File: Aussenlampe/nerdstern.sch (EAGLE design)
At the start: 14 parts, among them K1 G6RS

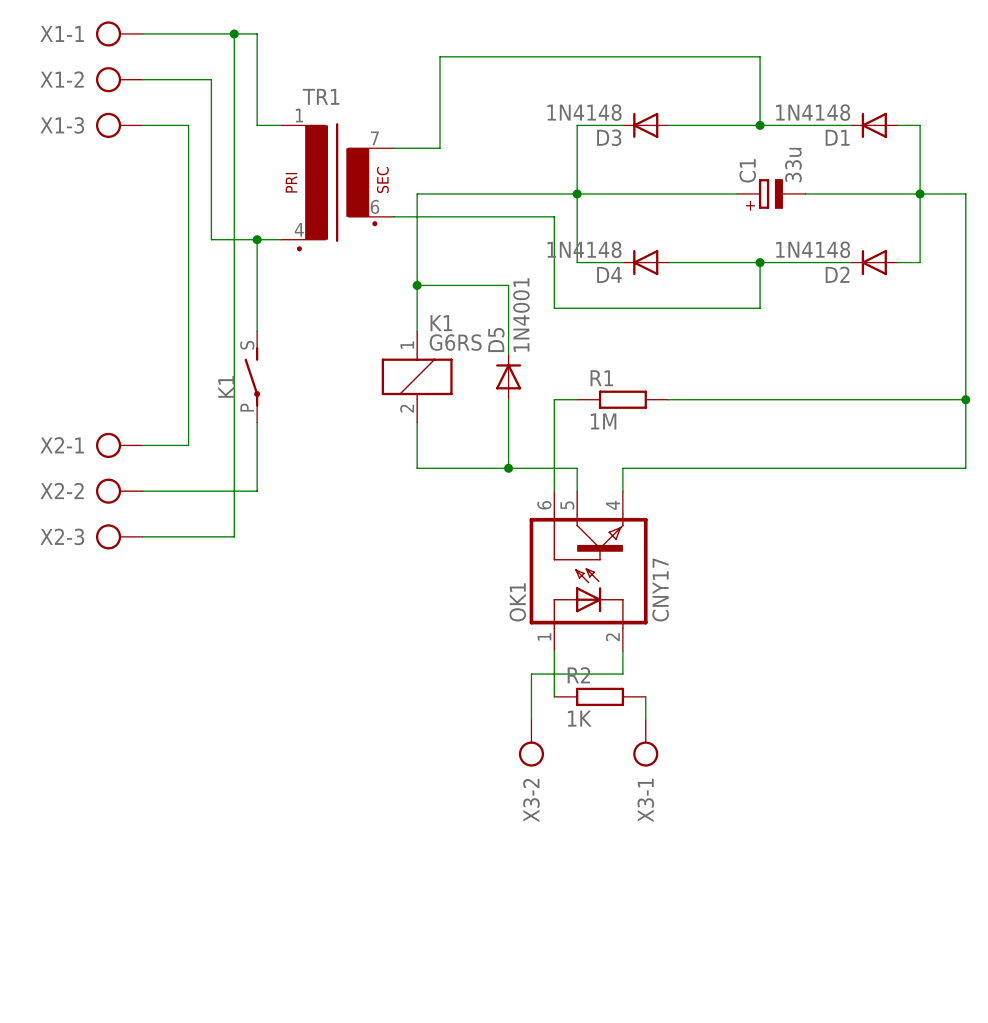
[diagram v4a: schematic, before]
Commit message: modified .gitignore
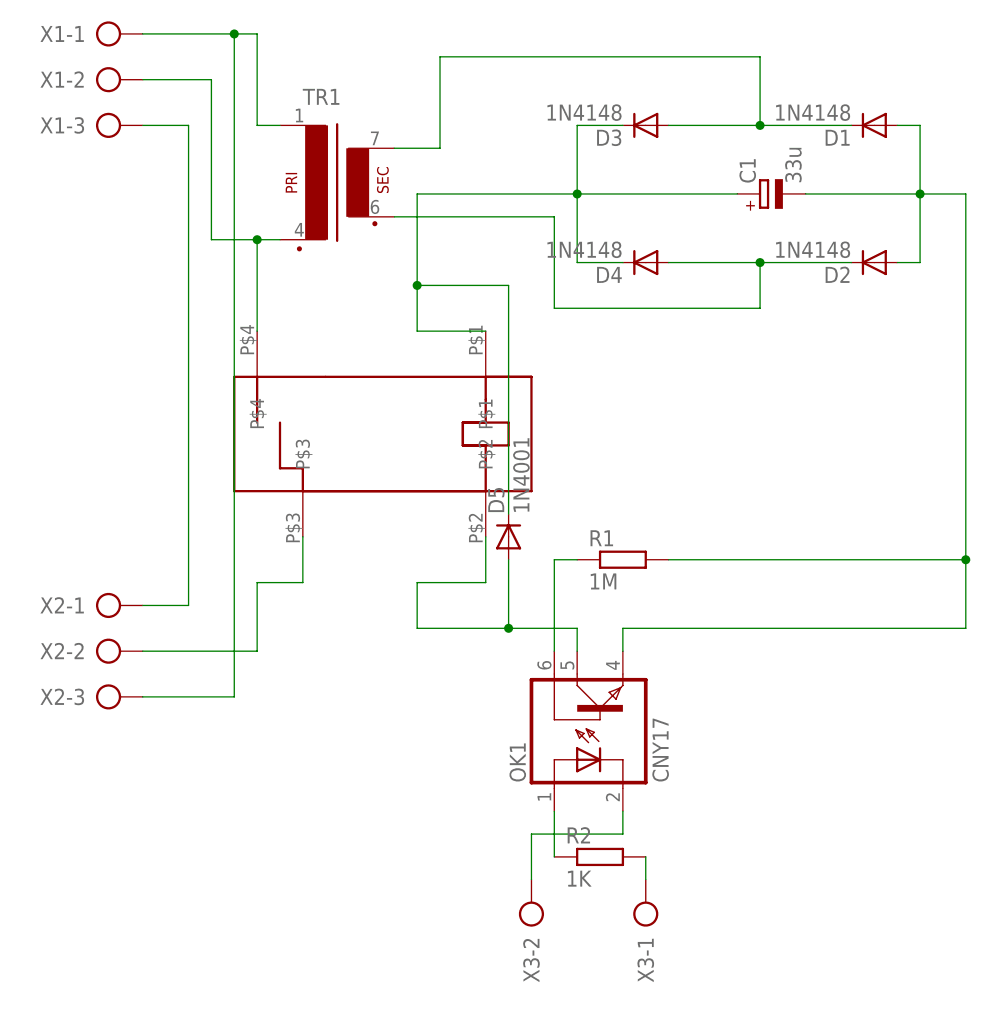
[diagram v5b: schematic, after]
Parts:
- removed K1: G6RS, relay:G6RS
- added U$1: JS_05_MN_KT, n39:JS_05_MN_KT
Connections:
- removed net N$12: D5.A, K11.2, OK1.COL
- new net N$6: D5.A, OK1.COL, U$1.P$2
- net N$1: now also U$1.P$4; no longer K12.S
- net N$2: now also U$1.P$3; no longer K12.P
- net N$5: now also U$1.P$1; no longer K11.1
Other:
- moved on the sheet: D5, OK1, R1, R2, X2-1, X2-2, X2-3, X3-1, X3-2
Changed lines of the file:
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@@
 <part name="D4" library="diode" deviceset="1N4148" device="DO35-7" value="1N4148"/>
 <part name="C1" library="rcl" deviceset="CPOL-EU" device="E2-5" value="33u"/>
-<part name="K1" library="relay" deviceset="G6RS" device=""/>
 <part name="X1" library="con-ptr500" deviceset="AK500/3" device=""/>
 <part name="X2" library="con-ptr500" deviceset="AK500/3" device=""/>
@@
 <part name="R2" library="rcl" deviceset="R-EU_" device="0204/5" value="1K"/>
 <part name="D5" library="diode" deviceset="1N4148" device="DO35-7" value="1N4001"/>
+<part name="U$1" library="n39" deviceset="JS_05_MN_KT" device=""/>
 </parts>
 <sheets>
@@
 <instance part="D4" gate="G$1" x="66.04" y="58.42" rot="R180"/>
 <instance part="C1" gate="G$1" x="78.74" y="66.04" rot="R90"/>
-<instance part="K1" gate="1" x="40.64" y="45.72"/>
-<instance part="K1" gate="2" x="22.86" y="45.72"/>
 <instance part="X1" gate="-1" x="5.08" y="83.82"/>
 <instance part="X1" gate="-2" x="5.08" y="78.74"/>
 <instance part="X1" gate="-3" x="5.08" y="73.66"/>
-<instance part="X2" gate="-1" x="5.08" y="38.1"/>
-<instance part="X2" gate="-2" x="5.08" y="33.02"/>
-<instance part="X2" gate="-3" x="5.08" y="27.94"/>
-<instance part="X3" gate="-1" x="66.04" y="2.54" rot="R90"/>
-<instance part="X3" gate="-2" x="53.34" y="2.54" rot="R90"/>
-<instance part="OK1" gate="G$1" x="58.42" y="25.4" rot="R90"/>
-<instance part="R1" gate="G$1" x="63.5" y="43.18"/>
-<instance part="R2" gate="G$1" x="60.96" y="10.16"/>
-<instance part="D5" gate="G$1" x="50.8" y="45.72" rot="R90"/>
+<instance part="X2" gate="-1" x="5.08" y="20.32"/>
+<instance part="X2" gate="-2" x="5.08" y="15.24"/>
+<instance part="X2" gate="-3" x="5.08" y="10.16"/>
+<instance part="X3" gate="-1" x="66.04" y="-15.24" rot="R90"/>
+<instance part="X3" gate="-2" x="53.34" y="-15.24" rot="R90"/>
+<instance part="OK1" gate="G$1" x="58.42" y="7.62" rot="R90"/>
+<instance part="R1" gate="G$1" x="63.5" y="25.4"/>
+<instance part="R2" gate="G$1" x="60.96" y="-7.62"/>
+<instance part="D5" gate="G$1" x="50.8" y="27.94" rot="R90"/>
+<instance part="U$1" gate="G$1" x="53.34" y="45.72" rot="R180"/>
 </instances>
 <busses>
@@
 <pinref part="TR1" gate="1" pin="P2"/>
 <wire x1="17.78" y1="60.96" x2="22.86" y2="60.96" width="0.1524" layer="91"/>
-<pinref part="K1" gate="2" pin="S"/>
 <wire x1="22.86" y1="50.8" x2="22.86" y2="60.96" width="0.1524" layer="91"/>
 <wire x1="22.86" y1="60.96" x2="25.4" y2="60.96" width="0.1524" layer="91"/>
 <junction x="22.86" y="60.96"/>
+<pinref part="U$1" gate="G$1" pin="P$4"/>
 </segment>
 </net>
 <net name="N$2" class="0">
 <segment>
-<pinref part="K1" gate="2" pin="P"/>
-<wire x1="22.86" y1="40.64" x2="22.86" y2="33.02" width="0.1524" layer="91"/>
-<wire x1="22.86" y1="33.02" x2="10.16" y2="33.02" width="0.1524" layer="91"/>
+<wire x1="22.86" y1="22.86" x2="22.86" y2="15.24" width="0.1524" layer="91"/>
+<wire x1="22.86" y1="15.24" x2="10.16" y2="15.24" width="0.1524" layer="91"/>
 <pinref part="X2" gate="-2" pin="KL"/>
+<pinref part="U$1" gate="G$1" pin="P$3"/>
+<wire x1="22.86" y1="22.86" x2="27.94" y2="22.86" width="0.1524" layer="91"/>
+<wire x1="27.94" y1="22.86" x2="27.94" y2="27.94" width="0.1524" layer="91"/>
 </segment>
 </net>
@@
 <wire x1="22.86" y1="83.82" x2="20.32" y2="83.82" width="0.1524" layer="91"/>
 <wire x1="20.32" y1="83.82" x2="10.16" y2="83.82" width="0.1524" layer="91"/>
-<wire x1="20.32" y1="27.94" x2="20.32" y2="83.82" width="0.1524" layer="91"/>
+<wire x1="20.32" y1="10.16" x2="20.32" y2="83.82" width="0.1524" layer="91"/>
 <junction x="20.32" y="83.82"/>
 <pinref part="X2" gate="-3" pin="KL"/>
-<wire x1="20.32" y1="27.94" x2="10.16" y2="27.94" width="0.1524" layer="91"/>
+<wire x1="20.32" y1="10.16" x2="10.16" y2="10.16" width="0.1524" layer="91"/>
 </segment>
 </net>
@@
 <net name="N$5" class="0">
 <segment>
-<pinref part="K1" gate="1" pin="1"/>
 <wire x1="40.64" y1="50.8" x2="40.64" y2="55.88" width="0.1524" layer="91"/>
 <pinref part="C1" gate="G$1" pin="+"/>
@@
 <wire x1="40.64" y1="66.04" x2="58.42" y2="66.04" width="0.1524" layer="91"/>
 <junction x="58.42" y="66.04"/>
-<wire x1="50.8" y1="48.26" x2="50.8" y2="55.88" width="0.1524" layer="91"/>
+<wire x1="50.8" y1="30.48" x2="50.8" y2="55.88" width="0.1524" layer="91"/>
 <wire x1="50.8" y1="55.88" x2="40.64" y2="55.88" width="0.1524" layer="91"/>
 <junction x="40.64" y="55.88"/>
 <pinref part="D5" gate="G$1" pin="C"/>
+<pinref part="U$1" gate="G$1" pin="P$1"/>
+<wire x1="48.26" y1="50.8" x2="40.64" y2="50.8" width="0.1524" layer="91"/>
 </segment>
 </net>
@@
 <wire x1="96.52" y1="58.42" x2="93.98" y2="58.42" width="0.1524" layer="91"/>
 <wire x1="96.52" y1="66.04" x2="101.6" y2="66.04" width="0.1524" layer="91"/>
-<wire x1="101.6" y1="66.04" x2="101.6" y2="43.18" width="0.1524" layer="91"/>
+<wire x1="101.6" y1="66.04" x2="101.6" y2="25.4" width="0.1524" layer="91"/>
 <junction x="96.52" y="66.04"/>
 <pinref part="OK1" gate="G$1" pin="EMI"/>
-<wire x1="101.6" y1="43.18" x2="101.6" y2="35.56" width="0.1524" layer="91"/>
-<wire x1="63.5" y1="33.02" x2="63.5" y2="35.56" width="0.1524" layer="91"/>
-<wire x1="63.5" y1="35.56" x2="101.6" y2="35.56" width="0.1524" layer="91"/>
+<wire x1="101.6" y1="25.4" x2="101.6" y2="17.78" width="0.1524" layer="91"/>
+<wire x1="63.5" y1="15.24" x2="63.5" y2="17.78" width="0.1524" layer="91"/>
+<wire x1="63.5" y1="17.78" x2="101.6" y2="17.78" width="0.1524" layer="91"/>
 <pinref part="R1" gate="G$1" pin="2"/>
-<wire x1="68.58" y1="43.18" x2="101.6" y2="43.18" width="0.1524" layer="91"/>
-<junction x="101.6" y="43.18"/>
+<wire x1="68.58" y1="25.4" x2="101.6" y2="25.4" width="0.1524" layer="91"/>
+<junction x="101.6" y="25.4"/>
 </segment>
 </net>
@@
 <pinref part="X1" gate="-3" pin="KL"/>
 <wire x1="10.16" y1="73.66" x2="15.24" y2="73.66" width="0.1524" layer="91"/>
-<wire x1="15.24" y1="73.66" x2="15.24" y2="38.1" width="0.1524" layer="91"/>
+<wire x1="15.24" y1="73.66" x2="15.24" y2="20.32" width="0.1524" layer="91"/>
 <pinref part="X2" gate="-1" pin="KL"/>
-<wire x1="10.16" y1="38.1" x2="15.24" y2="38.1" width="0.1524" layer="91"/>
+<wire x1="15.24" y1="20.32" x2="10.16" y2="20.32" width="0.1524" layer="91"/>
 </segment>
 </net>
@@
 <segment>
 <pinref part="OK1" gate="G$1" pin="A"/>
-<wire x1="55.88" y1="15.24" x2="55.88" y2="10.16" width="0.1524" layer="91"/>
+<wire x1="55.88" y1="-2.54" x2="55.88" y2="-7.62" width="0.1524" layer="91"/>
 <pinref part="R2" gate="G$1" pin="1"/>
 </segment>
@@
 <segment>
 <pinref part="X3" gate="-2" pin="KL"/>
-<wire x1="53.34" y1="12.7" x2="53.34" y2="7.62" width="0.1524" layer="91"/>
+<wire x1="53.34" y1="-5.08" x2="53.34" y2="-10.16" width="0.1524" layer="91"/>
 <pinref part="OK1" gate="G$1" pin="C"/>
-<wire x1="63.5" y1="15.24" x2="63.5" y2="12.7" width="0.1524" layer="91"/>
-<wire x1="53.34" y1="12.7" x2="63.5" y2="12.7" width="0.1524" layer="91"/>
+<wire x1="63.5" y1="-2.54" x2="63.5" y2="-5.08" width="0.1524" layer="91"/>
+<wire x1="53.34" y1="-5.08" x2="63.5" y2="-5.08" width="0.1524" layer="91"/>
 </segment>
 </net>
@@
 <pinref part="R1" gate="G$1" pin="1"/>
 <pinref part="OK1" gate="G$1" pin="BAS"/>
-<wire x1="58.42" y1="43.18" x2="55.88" y2="43.18" width="0.1524" layer="91"/>
-<wire x1="55.88" y1="43.18" x2="55.88" y2="33.02" width="0.1524" layer="91"/>
-</segment>
-</net>
-<net name="N$12" class="0">
-<segment>
-<pinref part="K1" gate="1" pin="2"/>
-<wire x1="40.64" y1="40.64" x2="40.64" y2="35.56" width="0.1524" layer="91"/>
-<wire x1="40.64" y1="35.56" x2="50.8" y2="35.56" width="0.1524" layer="91"/>
+<wire x1="58.42" y1="25.4" x2="55.88" y2="25.4" width="0.1524" layer="91"/>
+<wire x1="55.88" y1="25.4" x2="55.88" y2="15.24" width="0.1524" layer="91"/>
+</segment>
+</net>
+<net name="N$15" class="0">
+<segment>
+<pinref part="X3" gate="-1" pin="KL"/>
+<wire x1="66.04" y1="-7.62" x2="66.04" y2="-10.16" width="0.1524" layer="91"/>
+<pinref part="R2" gate="G$1" pin="2"/>
+</segment>
+</net>
+<net name="N$6" class="0">
+<segment>
+<pinref part="U$1" gate="G$1" pin="P$2"/>
+<wire x1="40.64" y1="22.86" x2="48.26" y2="22.86" width="0.1524" layer="91"/>
+<wire x1="48.26" y1="22.86" x2="48.26" y2="27.94" width="0.1524" layer="91"/>
+<wire x1="40.64" y1="22.86" x2="40.64" y2="17.78" width="0.1524" layer="91"/>
+<wire x1="40.64" y1="17.78" x2="50.8" y2="17.78" width="0.1524" layer="91"/>
 <pinref part="OK1" gate="G$1" pin="COL"/>
-<wire x1="50.8" y1="35.56" x2="58.42" y2="35.56" width="0.1524" layer="91"/>
-<wire x1="58.42" y1="35.56" x2="58.42" y2="33.02" width="0.1524" layer="91"/>
-<wire x1="50.8" y1="43.18" x2="50.8" y2="35.56" width="0.1524" layer="91"/>
-<junction x="50.8" y="35.56"/>
+<wire x1="50.8" y1="17.78" x2="58.42" y2="17.78" width="0.1524" layer="91"/>
+<wire x1="58.42" y1="17.78" x2="58.42" y2="15.24" width="0.1524" layer="91"/>
+<wire x1="50.8" y1="25.4" x2="50.8" y2="17.78" width="0.1524" layer="91"/>
+<junction x="50.8" y="17.78"/>
 <pinref part="D5" gate="G$1" pin="A"/>
 </segment>
 </net>
-<net name="N$15" class="0">
-<segment>
-<pinref part="X3" gate="-1" pin="KL"/>
-<wire x1="66.04" y1="10.16" x2="66.04" y2="7.62" width="0.1524" layer="91"/>
-<pinref part="R2" gate="G$1" pin="2"/>
-</segment>
-</net>
